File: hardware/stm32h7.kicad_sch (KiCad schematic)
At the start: 29 parts, among them SW21 SW_Push, SW22 SW_Push, U3 STM32H723ZGTx, Y1 25MHz

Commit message: continue h7 revision
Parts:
- added C28: 1u, Capacitor_SMD:C_0402_1005Metric, symbol Device:C_Small_US
- added C29: 100n, Capacitor_SMD:C_0402_1005Metric, symbol Device:C_Small_US
- added J8: Conn_ARM_JTAG_SWD_10, Connector_PinHeader_1.27mm:PinHeader_2x05_P1.27mm_Vertical_SMD, symbol Connector:Conn_ARM_JTAG_SWD_10
- FB2: footprint Inductor_SMD:L_0402_1005Metric -> Inductor_SMD:L_0603_1608Metric
- Y1: LCSC PN (none) -> C9006
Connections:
- net +3.3V: now also U3.108 (VDD), U3.121 (VDD), U3.131 (VDD), U3.144 (VDD), U3.17 (VDD), U3.30 (VDD), U3.39 (VDD), U3.52 (VDD), U3.6 (VBAT), U3.62 (VDD), U3.72 (VDD), U3.84 (VDD), U3.95 (VDD33USB), C28.1, C29.1, J8.1 (VTref)
- net GND: now also C28.2, C29.2, J8.3 (GND), J8.5 (GND), J8.9 (GNDDetect)
- net NRST: now also J8.10 (~{RESET})
- net VDDA: now also U3.33 (VDDA)
- net SYS_MCLK: now reaches U3.1 (PE2)
- net SWDIO: now reaches U3.105 (PA13(JTMS)
- net SWDIO: now also J8.2 (SWDIO/TMS)
- net SWCLK: now reaches U3.109 (PA14(JTCK)
- net SWCLK: now also J8.4 (SWCLK/TCK)
- net SWO: now reaches U3.133 (PB3(JTDO)
- net SWO: now also J8.6 (SWO/TDO)
- net SCL: now reaches U3.139 (PB8)
- net SDA: now reaches U3.140 (PB9)
- net I2S_DOUT: now reaches U3.2 (PE3)
- net I2S_LRCLK: now reaches U3.3 (PE4)
- net I2S_DIN: now reaches U3.4 (PE5)
- net I2S_SCLK: now reaches U3.5 (PE6)
- no-connect marks 0 -> 3
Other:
- note added: "VBAT"

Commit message: reorganize and finish codec / power
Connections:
- net I2S_DIN: now also U3.5 (PE6); no longer U3.4 (PE5)
- net I2S_SCLK: now also U3.4 (PE5); no longer U3.5 (PE6)
- net USB_D-: now reaches U3.103 (PA11)
- net USB_D+: now reaches U3.104 (PA12)
- net SPI_SCK: now reaches U3.41 (PA5)
- net SPI_MISO: now reaches U3.42 (PA6)
- net SPI_MOSI: now reaches U3.43 (PA7)
- net TCS: now reaches U3.44 (PC4)
- net RST: now reaches U3.45 (PC5)
- net DC: now reaches U3.46 (PB0)

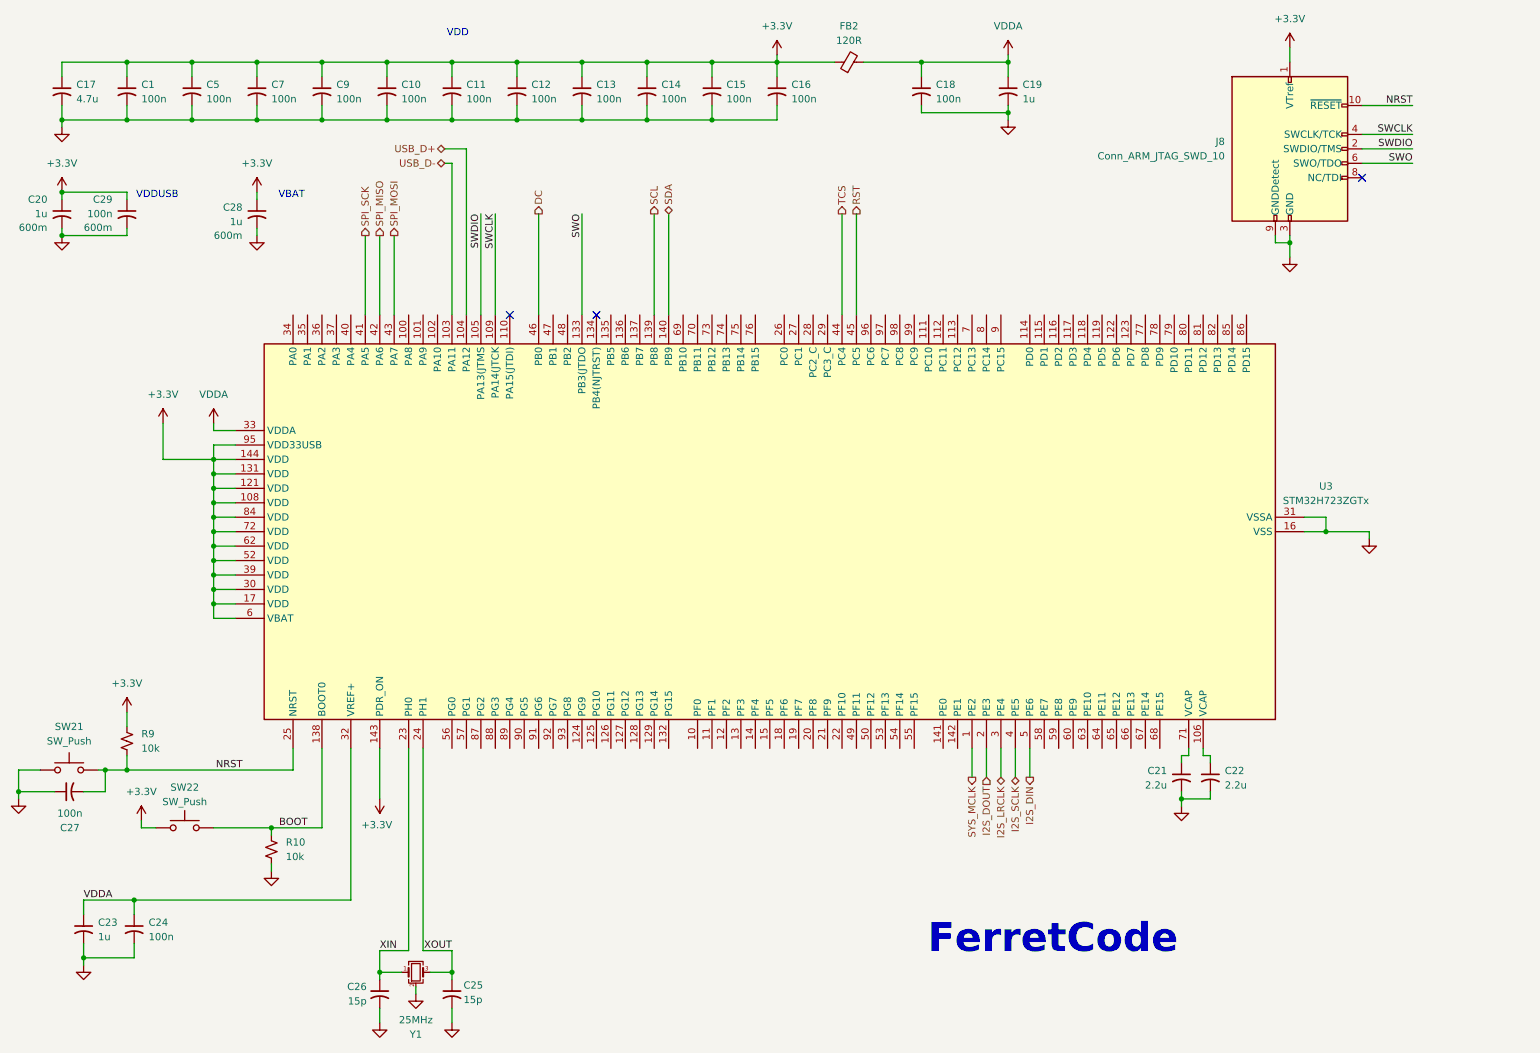
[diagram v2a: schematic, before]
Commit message: start rearranging layout
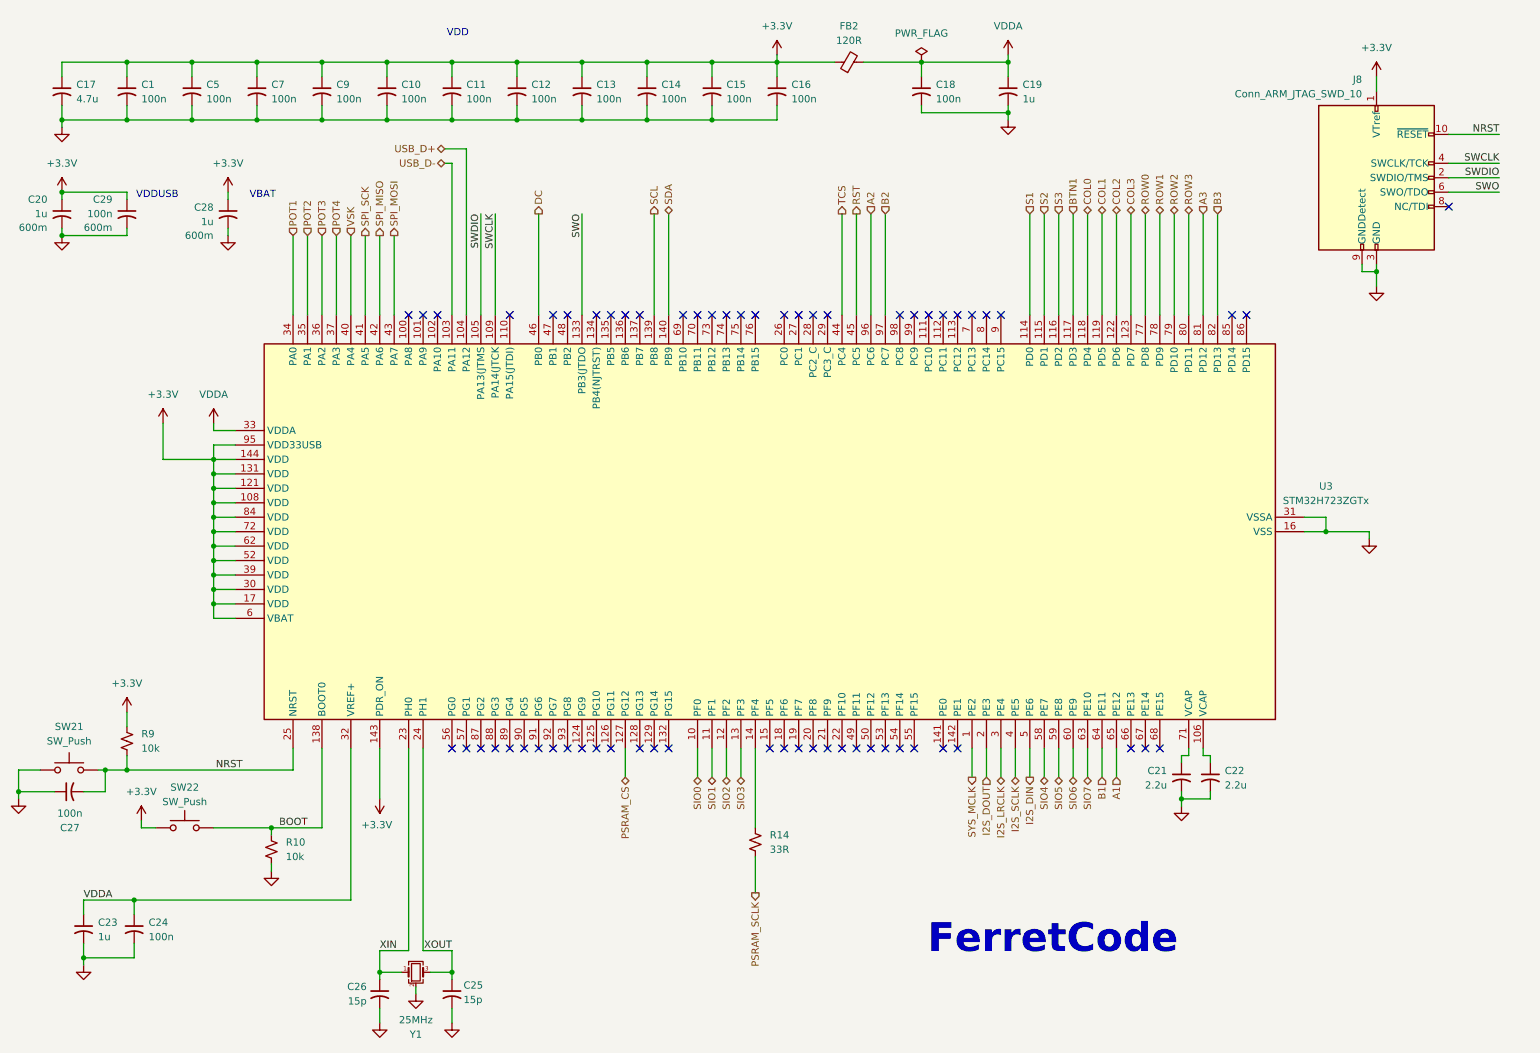
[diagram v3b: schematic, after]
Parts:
- added R14: 33R, Resistor_SMD:R_0402_1005Metric, symbol Device:R_Small_US
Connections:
- net SIO0: now reaches U3.10 (PF0)
- net SIO1: now reaches U3.11 (PF1)
- net S1: now reaches U3.114 (PD0)
- net S2: now reaches U3.115 (PD1)
- net S3: now reaches U3.116 (PD2)
- net BTN1: now reaches U3.117 (PD3)
- net COL0: now reaches U3.118 (PD4)
- net COL1: now reaches U3.119 (PD5)
- net SIO2: now reaches U3.12 (PF2)
- net COL2: now reaches U3.122 (PD6)
- net COL3: now reaches U3.123 (PD7)
- net PSRAM_CS: now reaches U3.127 (PG12)
- net SIO3: now reaches U3.13 (PF3)
- net at U3.14 (PF4): now also R14.1
- net POT1: now reaches U3.34 (PA0)
- net POT2: now reaches U3.35 (PA1)
- net POT3: now reaches U3.36 (PA2)
- net POT4: now reaches U3.37 (PA3)
- net VSK: now reaches U3.40 (PA4)
- net SIO4: now reaches U3.58 (PE7)
- net SIO5: now reaches U3.59 (PE8)
- net SIO6: now reaches U3.60 (PE9)
- net SIO7: now reaches U3.63 (PE10)
- net B1: now reaches U3.64 (PE11)
- net A1: now reaches U3.65 (PE12)
- net ROW0: now reaches U3.77 (PD8)
- net ROW1: now reaches U3.78 (PD9)
- net ROW2: now reaches U3.79 (PD10)
- net ROW3: now reaches U3.80 (PD11)
- net A3: now reaches U3.81 (PD12)
- net B3: now reaches U3.82 (PD13)
- net A2: now reaches U3.96 (PC6)
- net B2: now reaches U3.97 (PC7)
- new net PSRAM_SCLK: R14.2
- no-connect marks 3 -> 62
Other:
- moved on the sheet: C28, J8

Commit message: finish placement, add sd, codec routing
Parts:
- added R21: 33R, Resistor_SMD:R_0402_1005Metric, symbol Device:R_Small_US
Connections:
- net S3: now also U3.85 (PD14); no longer U3.116 (PD2)
- net DAT2: now reaches U3.111 (PC10)
- net DAT3: now reaches U3.112 (PC11)
- net at U3.113 (PC12): now also R21.2
- net DET_A: now reaches U3.87 (PG2)
- net DAT0: now reaches U3.98 (PC8)
- net DAT1: now reaches U3.99 (PC9)
- new net CLK: R21.1
- new net CMD: U3.116 (PD2)
- no-connect marks 62 -> 55
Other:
- added sheet SD Card (sd_card.kicad_sch)

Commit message: finish layout
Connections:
- net A1: now also U3.92 (PG7); no longer U3.65 (PE12)
- net A2: now also U3.88 (PG3); no longer U3.96 (PC6)
- net B1: now also U3.91 (PG6); no longer U3.64 (PE11)
- net B2: now also U3.89 (PG4); no longer U3.97 (PC7)
- net COL0: now also U3.123 (PD7); no longer U3.118 (PD4)
- net COL1: now also U3.122 (PD6); no longer U3.119 (PD5)
- net COL2: now also U3.119 (PD5); no longer U3.122 (PD6)
- net COL3: now also U3.118 (PD4); no longer U3.123 (PD7)
- net S1: now also U3.93 (PG8); no longer U3.114 (PD0)
- net S2: now also U3.90 (PG5); no longer U3.115 (PD1)

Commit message: finalize respin
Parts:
- C1, C10, C11, C12, C13, C14, C15, C16, C18, C24, C27, C29, C5, C7, C9: LCSC PN (none) -> C1525
- C17: LCSC PN (none) -> C23733
- C19, C20, C23, C28: LCSC PN (none) -> C52923
- C21, C22: LCSC PN (none) -> C23630
- C25, C26: LCSC PN (none) -> C1548
- FB2: LCSC PN (none) -> C14709
- J8: LCSC PN (none) -> C598540
- R10, R9: LCSC PN (none) -> C25744
- R14, R21: LCSC PN (none) -> C25105
- SW21, SW22: LCSC PN C115357 -> C202388
- U3: LCSC PN (none) -> C730146
